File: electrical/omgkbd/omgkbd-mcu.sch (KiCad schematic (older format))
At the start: 0 parts

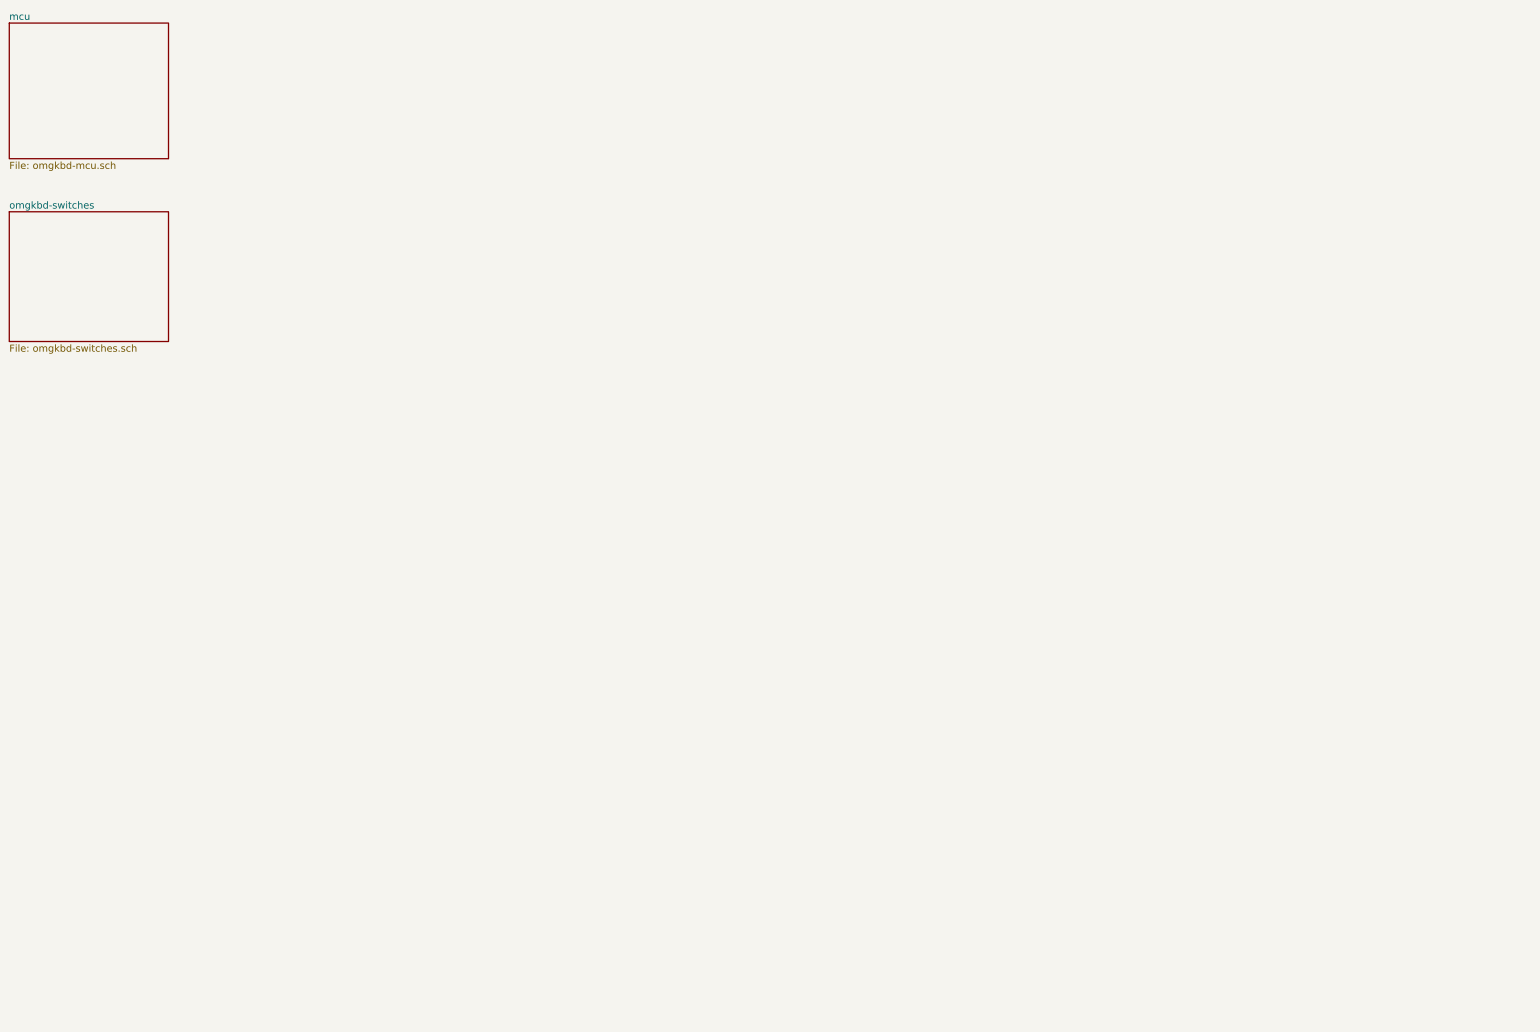
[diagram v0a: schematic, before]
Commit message: Added switches and MCU schematics
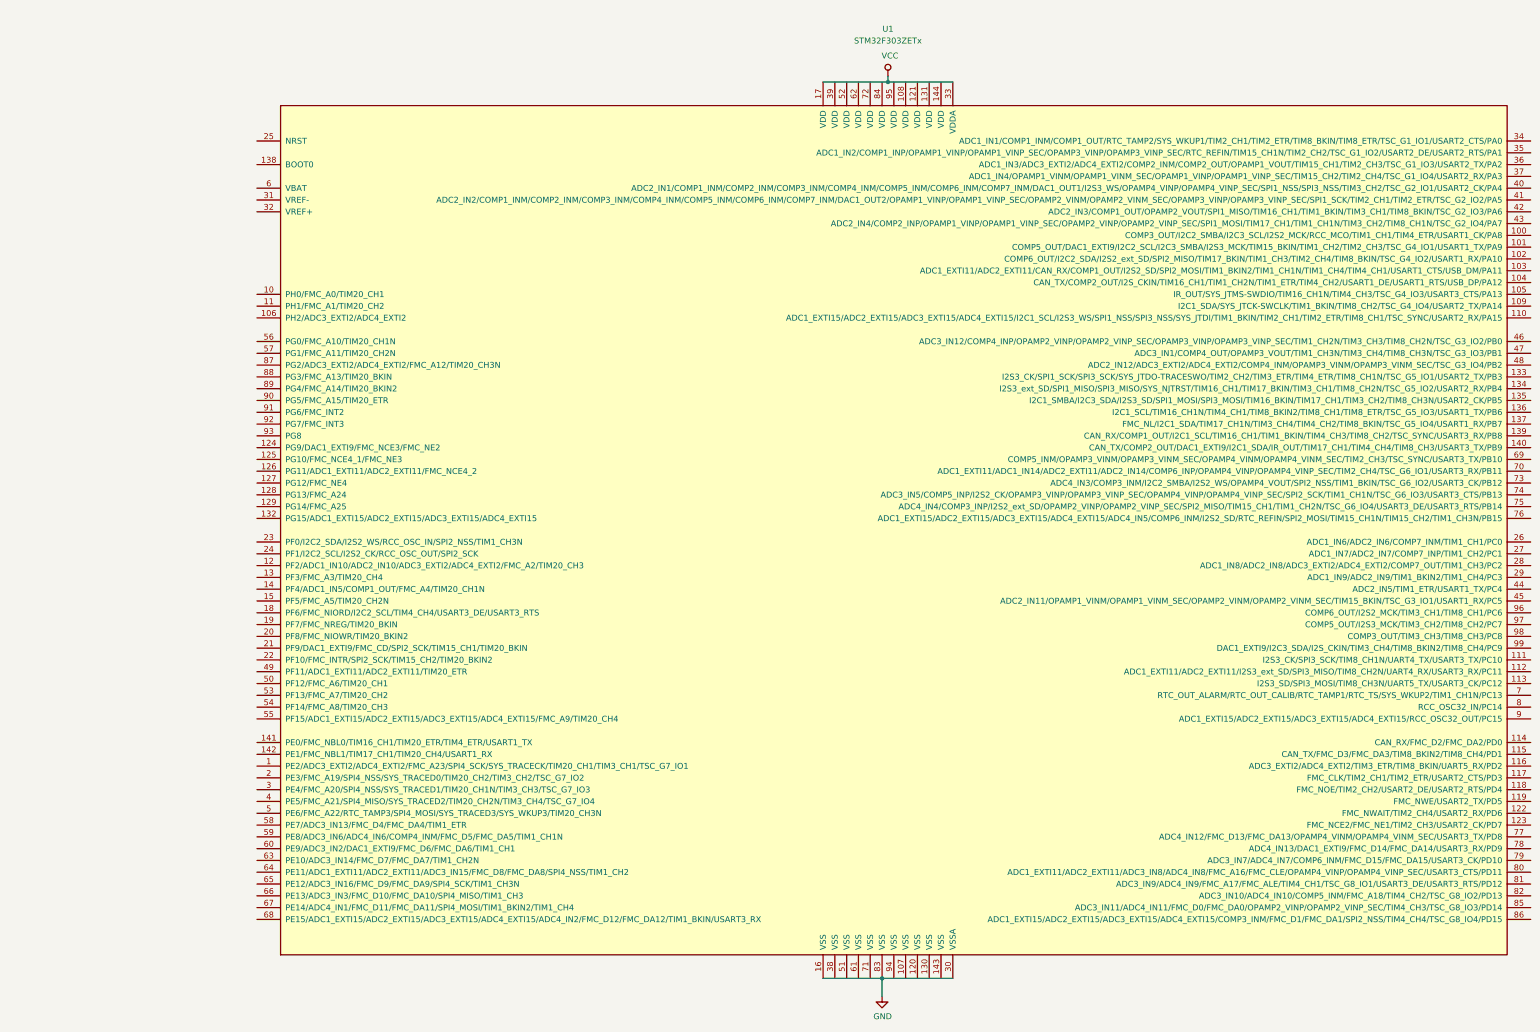
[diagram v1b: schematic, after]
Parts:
- added U1: STM32F303ZETx, Housings_QFP:LQFP-144_20x20mm_Pitch0.5mm, symbol STM32F303ZETx
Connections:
- new net GND: U1.16 (VSS), U1.30 (VSSA), U1.83 (VSS)
- new net VCC: U1.17 (VDD), U1.33 (VDDA)
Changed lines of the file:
@@
 $Descr A3 16535 11693
 encoding utf-8
-Sheet 1 3
+Sheet 2 3
 Title "Jellyfish"
 Date "2017-10-29"
@@
 Comment4 ""
 $EndDescr
-$Sheet
-S 800  850  1350 1150
-U 59F6280A
-F0 "mcu" 60
-F1 "omgkbd-mcu.sch" 60
-$EndSheet
-$Sheet
-S 800  2450 1350 1100
-U 59F8CCCC
-F0 "omgkbd-switches" 60
-F1 "omgkbd-switches.sch" 60
-$EndSheet
+$Comp
+L STM32F303ZETx U1
+U 1 1 59F23773
+P 8300 5150
+F 0 "U1" H 8250 9400 50  0000 C CNN
+F 1 "STM32F303ZETx" H 8250 9300 50  0000 C CNN
+F 2 "Housings_QFP:LQFP-144_20x20mm_Pitch0.5mm" H 13500 8725 50  0001 R TNN
+F 3 "http://www.st.com/content/ccc/resource/technical/document/datasheet/2c/6f/d7/64/1f/a3/4f/c9/DM00118585.pdf/files/DM00118585.pdf/jcr:content/translations/en.DM00118585.pdf" H 8300 5150 50  0001 C CNN
+	1    8300 5150
+	1    0    0    -1
+$EndComp
+$Comp
+L GND #PWR?
+U 1 1 59F628DB
+P 8200 9100
+F 0 "#PWR?" H 8200 8850 50  0001 C CNN
+F 1 "GND" H 8205 8927 50  0000 C CNN
+F 2 "" H 8200 9100 50  0001 C CNN
+F 3 "" H 8200 9100 50  0001 C CNN
+	1    8200 9100
+	1    0    0    -1
+$EndComp
+Wire Wire Line
+	7700 8950 8800 8950
+Wire Wire Line
+	8200 9100 8200 8950
+Connection ~ 8200 8950
+Wire Wire Line
+	8800 1350 7700 1350
+$Comp
+L VCC #PWR?
+U 1 1 59F62963
+P 8250 1300
+F 0 "#PWR?" H 8250 1150 50  0001 C CNN
+F 1 "VCC" H 8267 1473 50  0000 C CNN
+F 2 "" H 8250 1300 50  0001 C CNN
+F 3 "" H 8250 1300 50  0001 C CNN
+	1    8250 1300
+	1    0    0    -1
+$EndComp
+Wire Wire Line
+	8250 1300 8250 1350
+Connection ~ 8250 1350
 $EndSCHEMATC

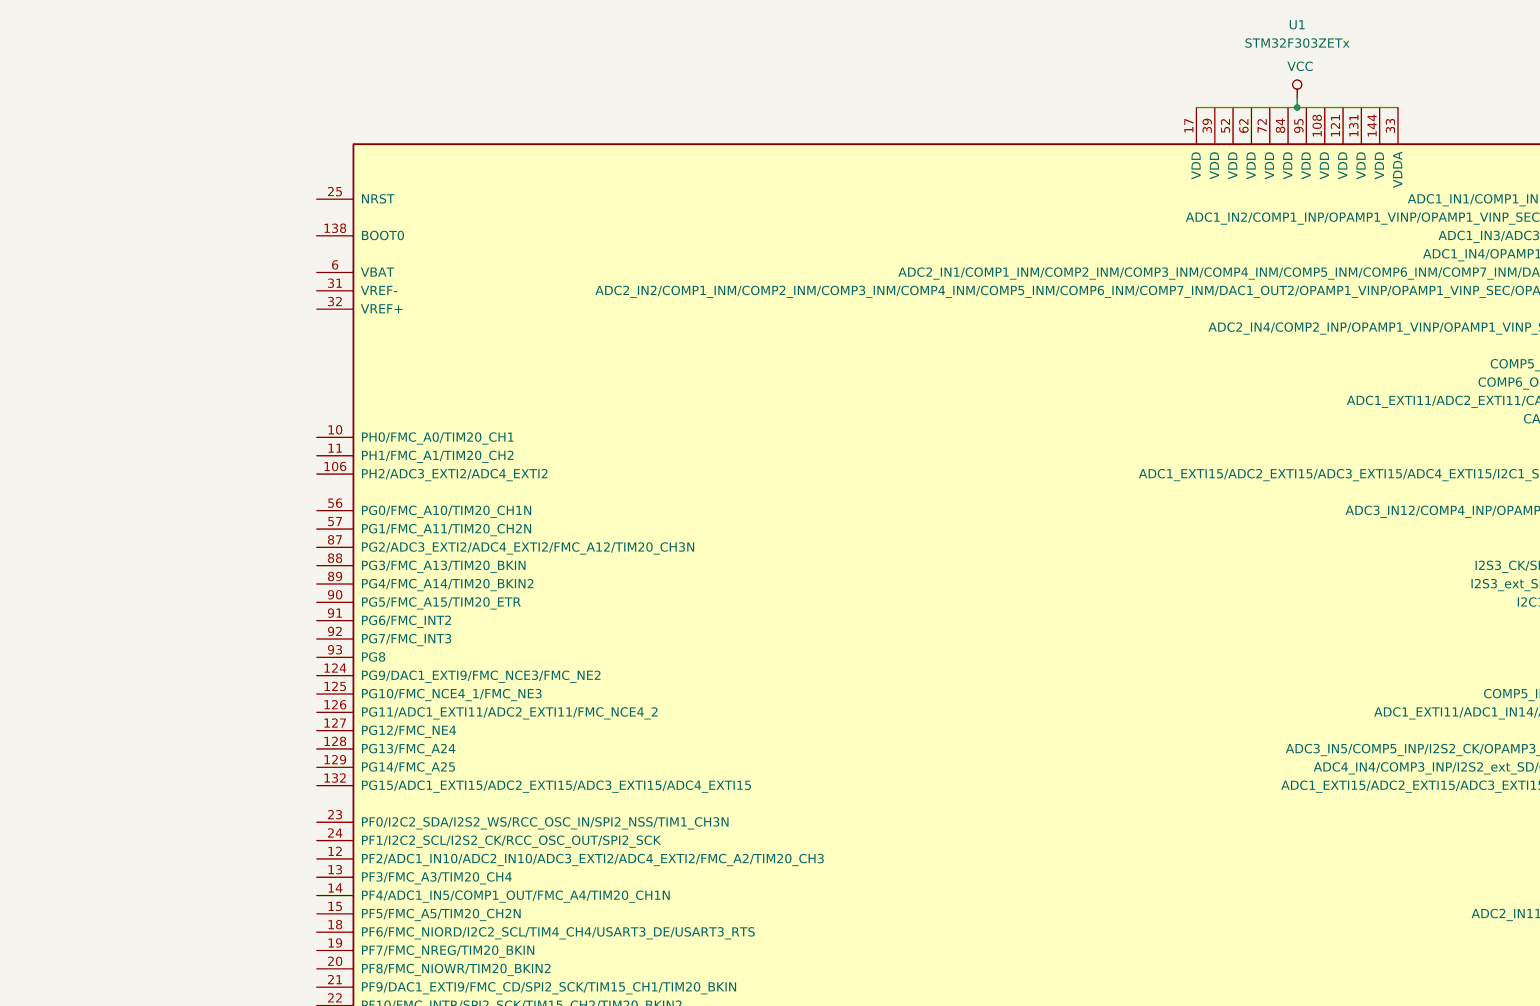
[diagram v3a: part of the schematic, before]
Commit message: Added crystal and some capacitors
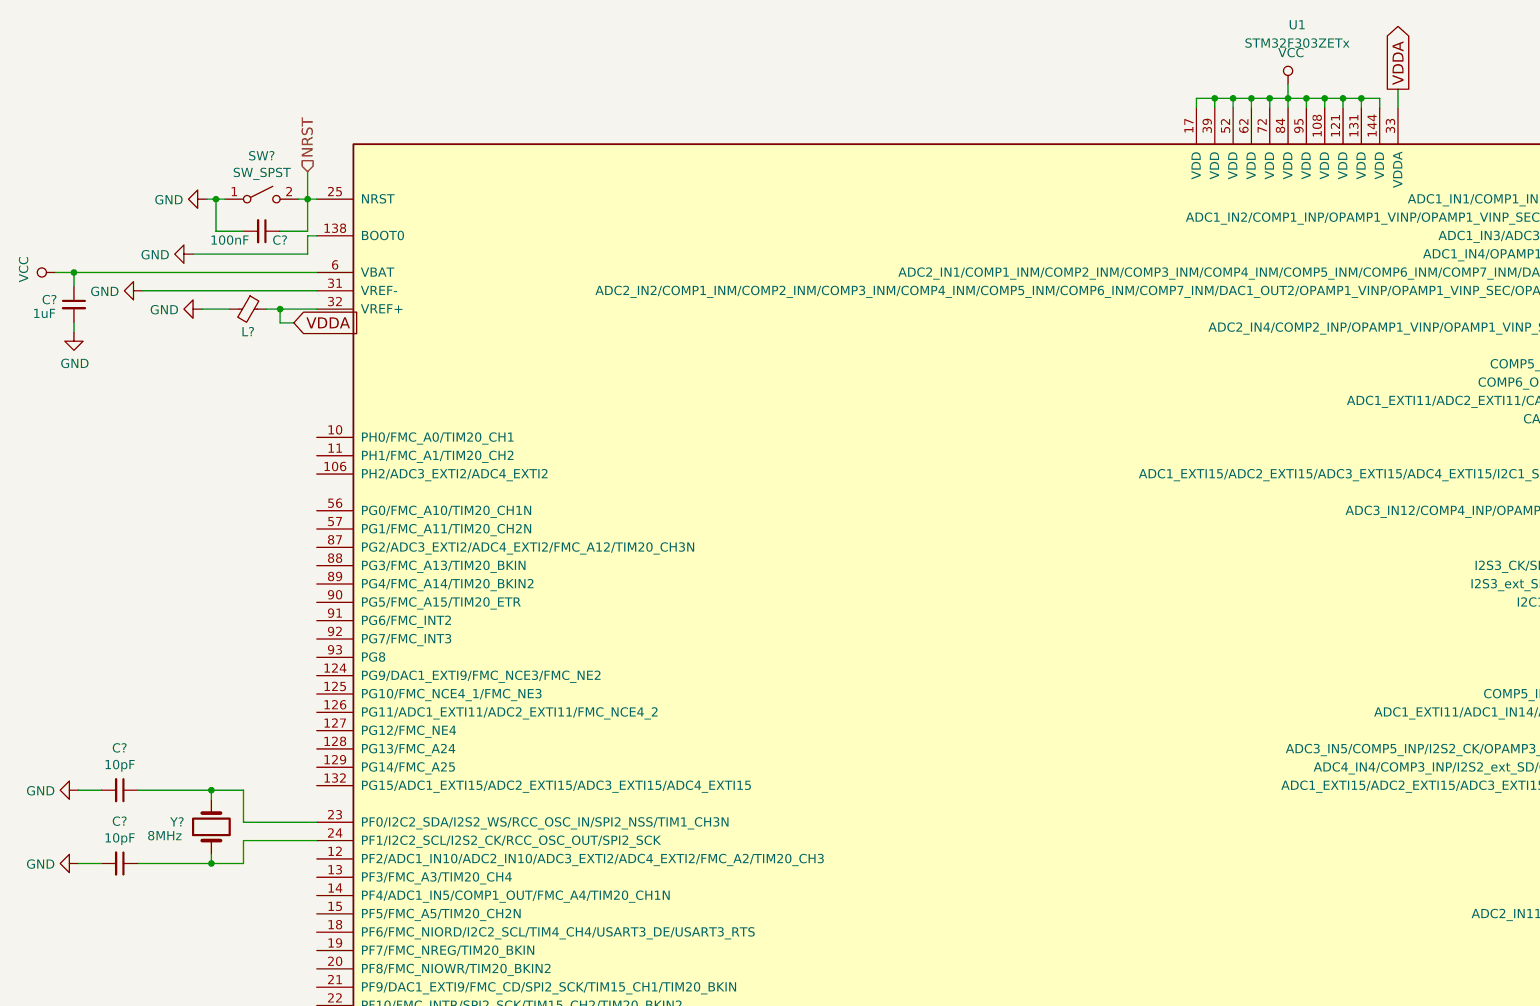
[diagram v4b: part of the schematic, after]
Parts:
- added C?: 1uF, symbol C_Small
- added C?: 100nF, symbol C_Small
- added C? (x2): 10pF, Capacitors_SMD:C_0805_HandSoldering, symbol C_Small
- added L?: Bead 470R, Inductors_SMD:L_0603_HandSoldering, symbol Ferrite_Bead_Small
- added SW?: SW_SPST, SeeedOPL-Switch-2016:SW4-6.0X6.0X5.0MM, symbol SW_SPST
- added Y?: 8MHz, Crystals:Crystal_SMD_HC49-SD_HandSoldering, symbol Crystal
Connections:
- net GND: now also U1.138 (BOOT0), U1.31 (VREF-), C?.2, C?.2, C?.2, C?.2, L?.2, SW?.1 (A)
- net VCC: now also U1.108 (VDD), U1.121 (VDD), U1.131 (VDD), U1.144 (VDD), U1.39 (VDD), U1.52 (VDD), U1.6 (VBAT), U1.62 (VDD), U1.72 (VDD), U1.84 (VDD), U1.95 (VDD), C?.1; no longer U1.33 (VDDA)
- net at U1.23 (PF0/I2C2_SDA/I2S2_WS/RCC_OSC_IN/SPI2_NSS/TIM1_CH3N): now also C?.1, Y?.2
- net at U1.24 (PF1/I2C2_SCL/I2S2_CK/RCC_OSC_OUT/SPI2_SCK): now also C?.1, Y?.1
- net NRST: now reaches U1.25 (NRST)
- net NRST: now also C?.1, SW?.2 (B)
- net VDDA: now reaches U1.32 (VREF+)
- net VDDA: now also U1.33 (VDDA), L?.1
